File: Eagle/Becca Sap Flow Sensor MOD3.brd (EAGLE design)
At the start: 63.1 x 49.1 mm, 59 parts, among them U1 V_REG_317SMD, U2 BORON, U6 RFM69HCW, U7 74HC4050D, U8 AP2112K-3.3, X2 USB Type C, X4 BQ24074, X5 uFL/SMA

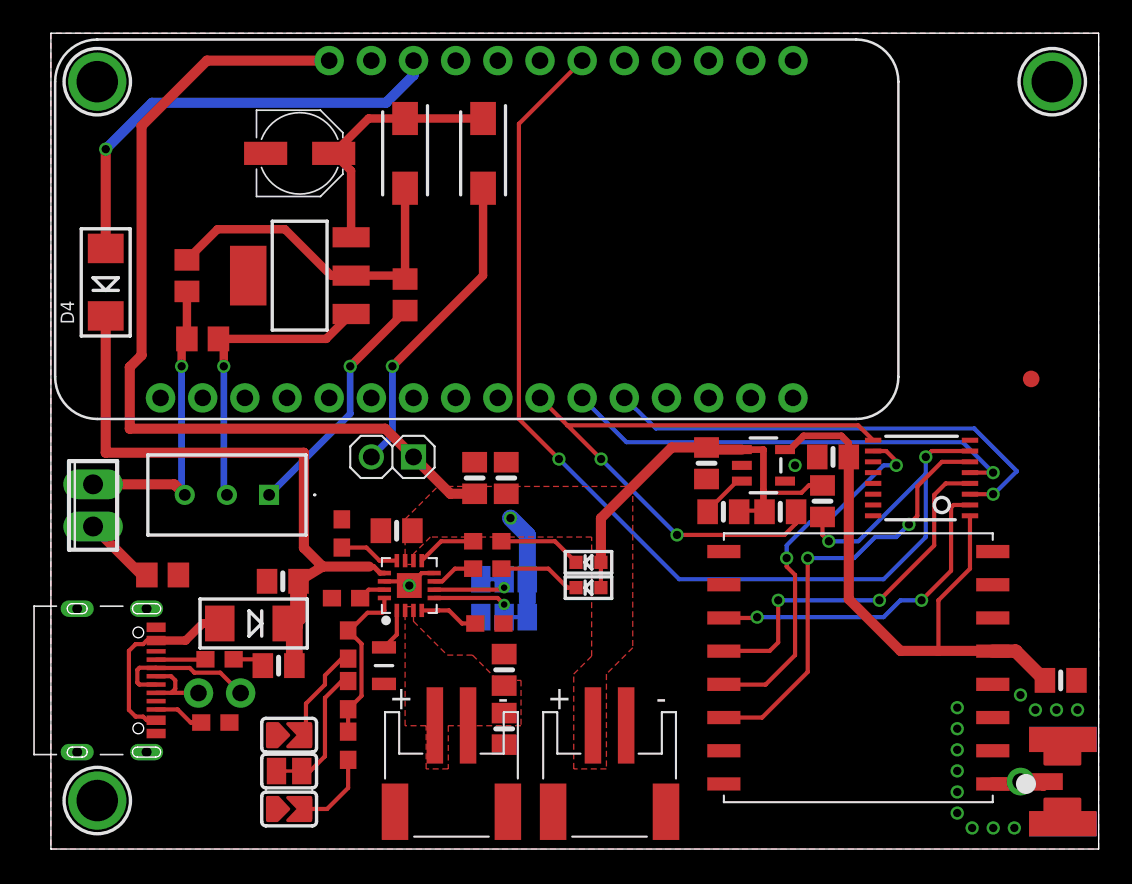
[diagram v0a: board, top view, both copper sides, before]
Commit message: Amended git ignore, also adding most recent sch
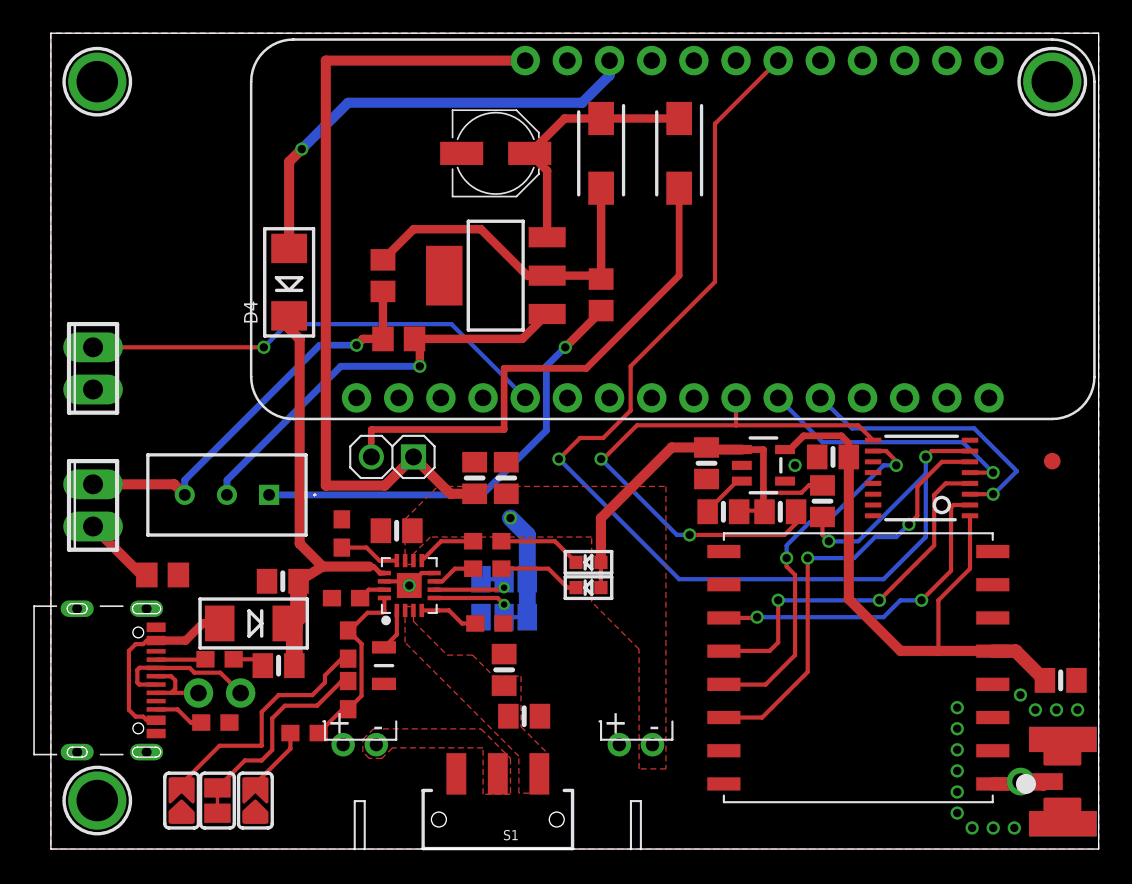
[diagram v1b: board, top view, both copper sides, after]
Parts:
- added S1: (no value), SparkFun-Retired:SWITCH_SPDT_SMD
- added X3: (no value), con-phoenix-254:2POL254
- BATT, SYSOUT: device adafruit:JST-PH-2-SMT-RA -> adafruit:JST-PH-2-THM-RA
- moved C7 11.8 mm to (26.8, 41.9)
- moved D6 11.8 mm to (33.1, 41.9)
- moved R12 11.8 mm to (33.1, 33.4)
- moved U1 11.8 mm to (26.8, 34.5)
- moved U2 11.8 mm to (62.9, 25.9)
- moved R10 11.8 mm to (20.0, 34.5)
- moved R13 11.8 mm to (21.0, 30.7)
- moved D5 11.8 mm to (37.8, 41.9)
- moved D4 11.0 mm to (14.4, 34.2)
- moved 1.5A 7.58 mm to (7.87, 2.92), turned to 90 degrees
- moved BATT 6.08 mm to (18.6, 6.29)
- moved FID2 5.11 mm to (60.3, 23.4)
- moved 1A 4.67 mm to (10.0, 2.92), turned to 90 degrees
- moved SYSOUT 3.00 mm to (35.2, 6.29)
- moved R5 2.74 mm to (15.3, 6.99), turned to 180 degrees
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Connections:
- new net N$17: U2.5, X3.2
- new net N$2: BATT.2, S1.2
- net GND: now also BATT.1, SYSOUT.1, X3.1; no longer BATT.2, SYSOUT.2
- net OUT: now also SYSOUT.2; no longer SYSOUT.1
- net VLIPO: now also S1.1; no longer BATT.1
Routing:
- net N$17: track 0.00 -> 28.5 mm, vias 0 -> 1
- net N$10: track 19.0 -> 31.5 mm, vias 1 -> 0
- net N$15: track 14.5 -> 26.9 mm
- net SCK_5V1: track 28.0 -> 16.2 mm
- net MOSI_5V1: track 28.9 -> 17.1 mm
- net VBUS: track 38.9 -> 27.3 mm
- net N$5: track 5.89 -> 14.6 mm
- net N$14: track 18.2 -> 25.7 mm
- net N$16: track 18.3 -> 25.0 mm
- net OUT: track 85.1 -> 79.5 mm
- net CS_5V1: track 38.6 -> 33.9 mm
- net N$7: track 7.10 -> 11.7 mm
- net RST_5V1: track 69.5 -> 73.2 mm
- net ISET: track 10.2 -> 11.2 mm
- net N$6: track 4.76 -> 3.92 mm
- added copper zone on layer 1, net N$2
